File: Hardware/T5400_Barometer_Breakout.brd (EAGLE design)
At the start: 25.4 x 14 mm, 13 parts, among them U1 T5400

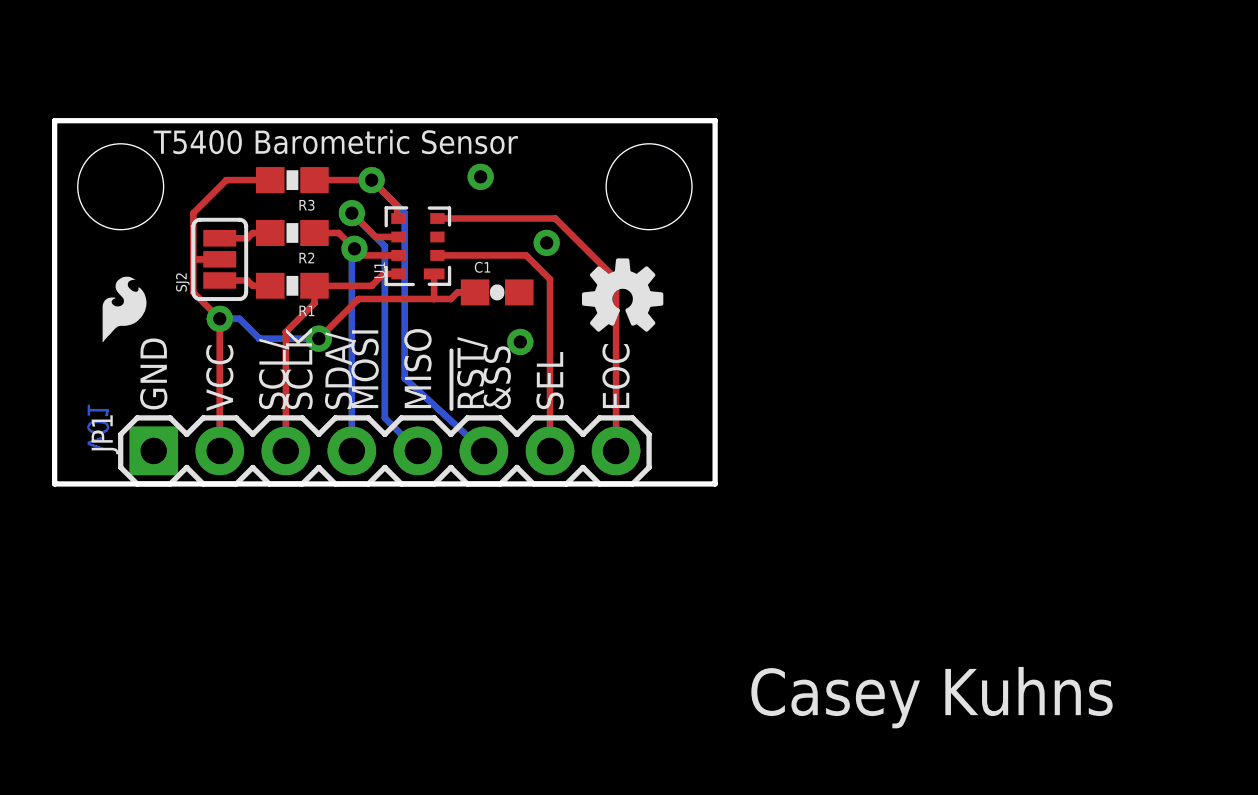
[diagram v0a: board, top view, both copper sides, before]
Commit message: updated with mode pullup and larger board
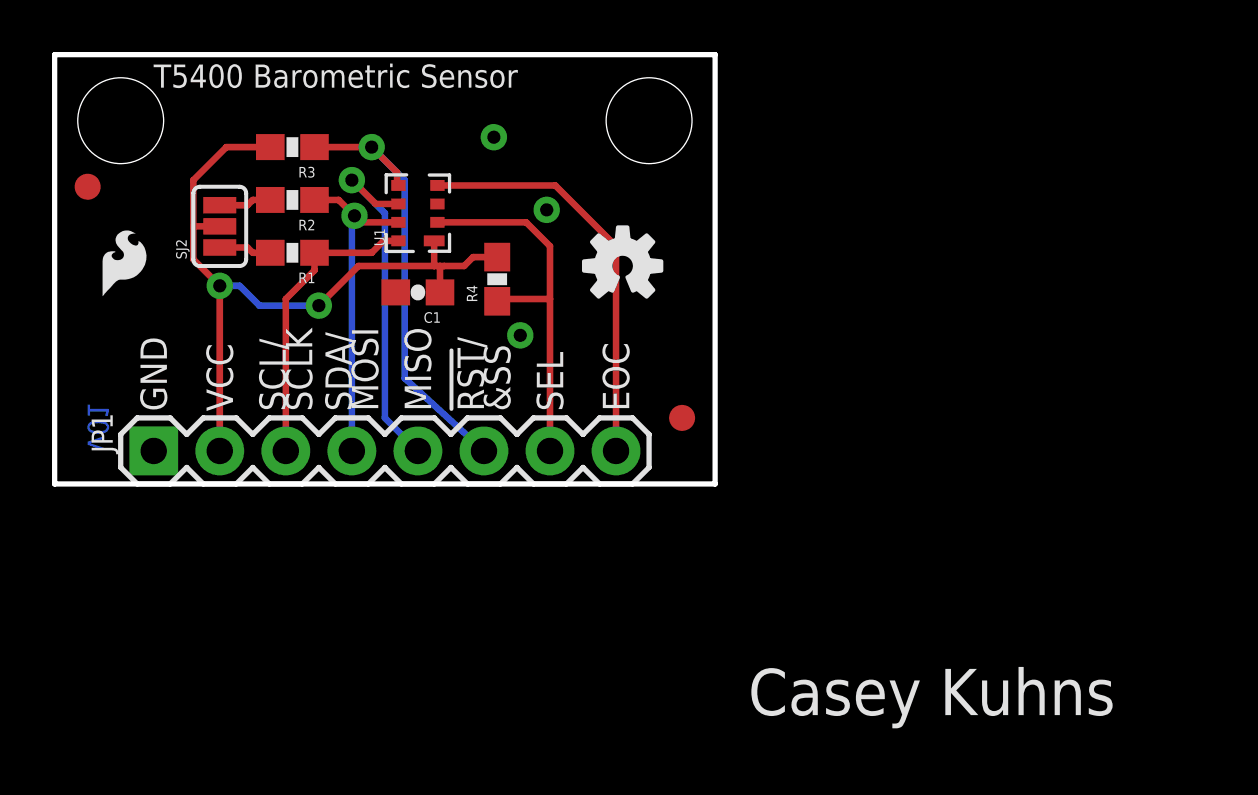
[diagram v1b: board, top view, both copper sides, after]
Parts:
- added FID1, FID2: FIDUCIAL1X2, SparkFun-Aesthetics:FIDUCIAL-1X2
- added R4: 10k, SparkFun-Passives:0603-RES
- moved C1 3.05 mm to (14.0, 7.37), turned to 180 degrees
- moved STANDOFF1 2.54 mm to (2.54, 14.0)
- moved STANDOFF2 2.54 mm to (22.9, 14.0)
- moved LOGO3 1.78 mm to (1.52, 6.86)
- moved R2 1.27 mm to (9.14, 10.9)
- moved R3 1.27 mm to (9.14, 13.0)
- moved SJ2 1.27 mm to (6.35, 9.91)
- moved R1 1.27 mm to (9.14, 8.89)
- moved LOGO1 1.27 mm to (22.4, 7.37)
- moved LOGO2 1.27 mm to (21.8, 8.38)
- moved U1 1.27 mm to (14.0, 10.4)
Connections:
- net SEL: now also R4.1
- net VCC: now also R4.2
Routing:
- net SEL: track 11.3 -> 14.7 mm
- net VCC: track 25.9 -> 29.1 mm
- net SCL/SCLK: track 10.2 -> 11.5 mm
- net MISO: track 12.4 -> 13.6 mm
- net EOC: track 14.4 -> 15.7 mm
- net !RST!/&SS: track 16.5 -> 17.7 mm
- net SDA/MOSI: track 11.6 -> 12.9 mm
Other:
- board size 25.4 x 14 mm -> 25.4 x 16.5 mm

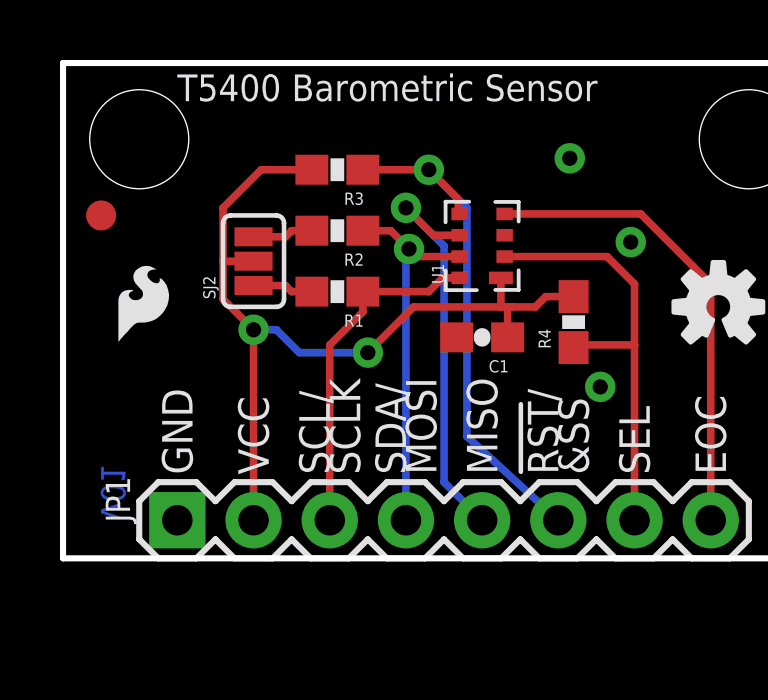
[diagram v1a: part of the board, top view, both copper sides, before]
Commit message: changed version and modified pads for production
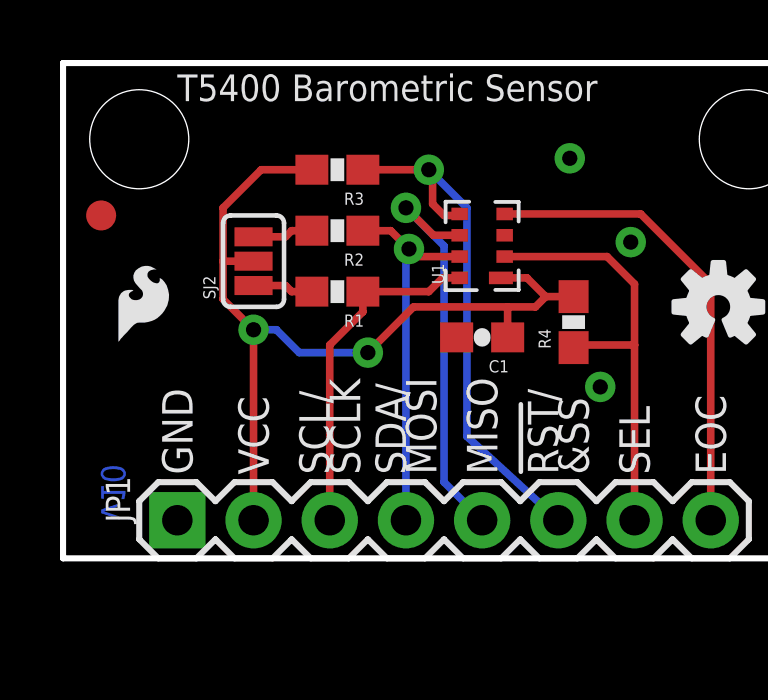
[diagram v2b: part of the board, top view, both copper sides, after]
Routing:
- net VCC: track 29.1 -> 29.9 mm
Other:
- board text added: "v10"
- board text removed: "v01"
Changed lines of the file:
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@@
 <setting verticaltext="up"/>
 </settings>
-<grid distance="0.05" unitdist="inch" unit="inch" style="lines" multiple="1" display="yes" altdistance="0.05" altunitdist="inch" altunit="inch"/>
+<grid distance="0.005" unitdist="inch" unit="inch" style="lines" multiple="1" display="yes" altdistance="0.05" altunitdist="inch" altunit="inch"/>
 <layers>
 <layer number="1" name="Top" color="4" fill="1" visible="yes" active="yes"/>
@@
 <text x="11.938" y="2.794" size="1.016" layer="21" font="vector" ratio="15" rot="R90" align="center-left">MOSI</text>
 <text x="17.018" y="2.794" size="1.016" layer="21" font="vector" ratio="15" rot="R90" align="center-left">&amp;SS</text>
-<text x="1.27" y="1.27" size="0.8128" layer="16" font="vector" ratio="25" rot="MR90">v01</text>
+<text x="1.27" y="1.27" size="0.8128" layer="16" font="vector" ratio="25" rot="MR90">v10</text>
 <text x="3.81" y="5.334" size="1.016" layer="22" font="vector" ratio="15" rot="SMR270" align="center-left">GND</text>
 <text x="6.35" y="5.334" size="1.016" layer="22" font="vector" ratio="15" rot="SMR270" align="center-left">VCC</text>
@@
 <rectangle x1="13.716" y1="8.89" x2="13.97" y2="9.652" layer="41"/>
 <rectangle x1="13.716" y1="9.652" x2="14.224" y2="10.414" layer="41"/>
+<text x="3.556" y="16.129" size="0.889" layer="22" font="vector" ratio="15" rot="MR180">T5400 Barometric Sensor</text>
 </plain>
 <attributes>
@@
 <via x="12.192" y="12.954" extent="1-16" drill="0.508"/>
 <wire x1="13.22" y1="11.479" x2="13.171" y2="11.43" width="0.254" layer="1"/>
-<wire x1="13.171" y1="11.43" x2="13.171" y2="11.975" width="0.254" layer="1"/>
-<wire x1="13.171" y1="11.975" x2="12.192" y2="12.954" width="0.254" layer="1"/>
 <wire x1="12.192" y1="12.954" x2="13.462" y2="11.684" width="0.254" layer="16"/>
 <wire x1="13.462" y1="11.684" x2="13.462" y2="4.064" width="0.254" layer="16"/>
 <wire x1="13.462" y1="4.064" x2="16.51" y2="1.27" width="0.254" layer="16"/>
+<wire x1="13.171" y1="11.43" x2="12.7" y2="11.43" width="0.254" layer="1"/>
+<wire x1="12.7" y1="11.43" x2="12.319" y2="11.811" width="0.254" layer="1"/>
+<wire x1="12.319" y1="11.811" x2="12.319" y2="12.827" width="0.254" layer="1"/>
+<wire x1="12.319" y1="12.827" x2="12.192" y2="12.954" width="0.254" layer="1"/>
 </signal>
 <signal name="MISO">
@@
 <via x="10.16" y="6.858" extent="1-16" drill="0.508"/>
 <wire x1="10.16" y1="6.858" x2="11.684" y2="8.382" width="0.254" layer="1"/>
-<wire x1="11.684" y1="8.382" x2="14.595" y2="8.382" width="0.254" layer="1"/>
-<wire x1="14.595" y1="9.349" x2="14.595" y2="8.382" width="0.254" layer="1"/>
+<wire x1="11.684" y1="8.382" x2="14.82" y2="8.382" width="0.254" layer="1"/>
 <wire x1="10.16" y1="6.858" x2="7.874" y2="6.858" width="0.254" layer="16"/>
 <wire x1="7.874" y1="6.858" x2="7.112" y2="7.62" width="0.254" layer="16"/>
@@
 <via x="6.35" y="7.62" extent="1-16" drill="0.508"/>
 <contactref element="R4" pad="2"/>
-<wire x1="14.595" y1="8.382" x2="14.82" y2="8.382" width="0.254" layer="1"/>
-<wire x1="14.986" y1="8.382" x2="15.748" y2="8.382" width="0.254" layer="1"/>
+<wire x1="14.82" y1="8.382" x2="15.748" y2="8.382" width="0.254" layer="1"/>
 <wire x1="17.018" y1="8.724" x2="16.09" y2="8.724" width="0.254" layer="1"/>
 <wire x1="16.09" y1="8.724" x2="15.748" y2="8.382" width="0.254" layer="1"/>
 <wire x1="14.82" y1="7.366" x2="14.82" y2="8.382" width="0.254" layer="1"/>
-<wire x1="14.82" y1="8.382" x2="14.986" y2="8.382" width="0.254" layer="1"/>
+<wire x1="14.595" y1="9.349" x2="15.465" y2="9.349" width="0.254" layer="1"/>
+<wire x1="15.465" y1="9.349" x2="16.09" y2="8.724" width="0.254" layer="1"/>
 </signal>
 <signal name="N$1">
